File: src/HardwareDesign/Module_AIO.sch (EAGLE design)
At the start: 284 parts, among them IC1 MIC5504-3.3YM5-TR, IC10 ADS9234RIRHBR, IC11 AD8605, IC12 MCP1525T-I/TT, IC13 AD8605, IC14 TPS65131, IC15 TPS7A39, IC16 SN74LVC2G66, IC17 74LVC1G04, IC22 DAC8568, IC23 AD8605, IC24 OPA192, IC25 OPA192, IC26 OPA192, IC27 OPA192, IC28 OPA197, IC29 OPA197, IC30 OPA197, IC31 OPA197, IC6 DG409, IC7 ADA4254ACPZ, IC8 DG409, IC9 ADA4254ACPZ, T2 IRLML5203, X1 MAB64

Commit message: AIO Board ready
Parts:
- removed SPI0_MISO, SPI0_MOSI, SPI0_SCK: TP, ds_passive:TP
- added AVDD, DVDD, IOVDD, VBUS, VREF1: TP, ds_passive:TP
- added C112, C113, C114, C116, C16, C17, C18, C77, C80, C81, C82, C83, C84, C87, C88, C89: 100nF, ds_passive:C-0402
- added C115: 4.7nF, ds_passive:C0402
- added C15: 1uF, ds_passive:C-0402
- added C19, C20: 15pF, ds_passive:C-0402
- added C78: 10uF, ds_passive:C0805
- added C79: 100nF, ds_passive:C0402
- added D1: SS12, Diodes:SS12
- added DBG1, DBG2: (no value), ds_con:CON-1X4
- added ESD1: SP0503BAHTG-ES, ds_ic_peripherals:SP0503BAHT
- added IC2: RP2040, ds_ic_mcu:RP2040
- added IC3: MCP6001AIDBVRG, ds_ic_opa:MCP6001RT
- added IC4: W25Q128JVPIQ, MCU:W25Q128JVP
- added J1: (no value), ds_con:N10236-52B3PC
- added JP-3V3-1, JP-3V3-2: 0R, ds_passive:R0603
- added R10, R11: 1K, ds_passive:R0402
- added R12: 2.2K 1%, ds_passive:R0402
- added R13, R39: 27R, ds_passive:R0402
- added R17, R72, R77: 4.7K, ds_passive:R0402
- added R18: DNI, ds_passive:R0402
- added R61, R62: 5.1K, ds_passive:R0402
- added R63, R64, R75: 10K, ds_passive:R0402
- added R67, R71: 10K 0.1%, ds_passive:R0402
- added R68: 1M, ds_passive:R0402
- added R69, R70: 100K 0.1%, ds_passive:R0402
- added R9: 0R, ds_passive:R0402
- added REF1: LM4040BXX, ds_ic_vreg:LM4040BXX
- added RESET, USB_BOOT: B3U-1000P-B, 52101-101-REV-A_v16:SWITCH-OMRON_B3U-1000P
- added USBC: USB-TYPE-C-018, Wurth_Connectors_WR-USB:629722000214
- added X2: K5A1200015304P, ds_passive:CRYSTAL
- C102, C104, C108, C109, C93, C94, C95, C96, C97, C98: device ds_passive:C-0402 -> ds_passive:C-0805
- R26, R27, R28, R29, R30, R31, R32, R34, R35, R36, R37, R38, R40, R41: device ds_passive:R0603 -> ds_passive:R0402
- R55, R56: value (none) -> 20K
- X1: value MAB64 -> CON-VG_MAB64; device con-vg:MAB64 -> ds_con:CON-VG_MAB64
- renumbered SPI0_CS0 to CS3, SPI1_CS0 to MOSI, SPI1_CS1 to MISO, SPI1_CS2 to SCK, SPI1_CS3 to CS0, SPI1_CS4 to CS1, SPI1_CS5 to CS2
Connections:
- removed net SPI1_CS0: IC10.!CS, MOSI.P$1, R15.1, X1A.2
- removed net SPI1_CS1: IC7.!CS, MISO.P$1, X1A.3
- removed net SPI1_CS2: IC9.!CS, SCK.P$1, X1A.4
- new net !QSPI_SS: IC2.QSPI_SS_N, IC4.!CS, R11.2, R18.1
- new net +1V1: C112.1, C113.1, C114.1, DVDD.P$1, IC2.DVDD, IC2.VREG_VOUT
- new net ADC_12VN: IC2.GPIO28/ADC2, R67.2, R69.1
- new net ADC_12VP: IC2.GPIO27/ADC1, R70.2, R71.1
- new net ADC_5VP: IC2.GPIO29/ADC3, R72.1, R77.2
- new net ADC_VUSB: IC2.GPIO26/ADC0, R63.2, R64.1
- new net AVDD: AVDD.P$1, C17.1, C89.1, IC2.ADC_AVDD, IC3.-IN, IC3.OUT
- new net CC1: R62.1, USBC.CC1
- new net CC2: R61.1, USBC.CC2
- new net EXT: J1.1, J1.20
- new net N$1: C20.1, R10.1, R9.2, X2.OUT
- new net N$4: JP-3V3-1.2, X1A.1
- new net N$6: JP-3V3-2.2, X1B.1
- new net QSPI_SCLK: IC2.QSPI_SCLK, IC4.CLK
- new net QSPI_SD0: IC2.QSPI_SD0, IC4.DI/IO0
- new net QSPI_SD1: IC2.QSPI_SD1, IC4.DO/IO1
- new net QSPI_SD2: IC2.QSPI_SD2, IC4.!WP!/IO2
- new net QSPI_SD3: IC2.QSPI_SD3, IC4.!HOLD!/IO3
- new net RP2040_RST: IC2.RUN, R75.2, RESET.P, X1B.18
- new net RP_USBD_N: IC2.USB_DM, R13.2
- new net RP_USBD_P: IC2.USB_DP, R39.2
- new net RP_XI: C19.1, IC2.XIN, R9.1, X2.CON
- new net RP_XO: IC2.XOUT, R10.2
- new net SDO_A_1: IC10.SDO-1/1A, IC2.GPIO17, X1A.18
- new net SDO_A_2: IC10.SDO-2/2A, IC2.GPIO18, X1A.19
- new net SDO_A_3: IC10.SDO-3/3A, IC2.GPIO19, X1A.20
- new net SDO_B_1: IC10.SDO-5/1B, IC2.GPIO21, X1A.22
- new net SDO_B_2: IC10.SDO-6/2B, IC2.GPIO22, X1A.23
- new net SDO_B_3: IC10.SDO-7/3B, IC2.GPIO23, X1A.24
- new net SPI0_CS1: CS1.P$1, IC2.GPIO6, IC7.!CS, X1A.3
- new net SPI0_CS2: CS2.P$1, IC2.GPIO7, IC9.!CS, X1A.4
- new net SPI0_CS3: CS3.P$1, IC2.GPIO25, IC22.!SYNC, R86.3, X1B.2
- new net SPI1_CS: IC2.GPIO13, X1A.29, X1B.29
- new net SWCLK: DBG2.P$1, IC2.SWCLK, X1B.23
- new net SWDIO: DBG2.P$3, IC2.SWDIO, X1B.24
- new net UART0_RX: DBG1.P$1, IC2.GPIO0, X1B.20
- new net UART0_TX: DBG1.P$3, IC2.GPIO1, X1B.21
- new net USBD_N: ESD1.C2, R13.1, USBC.D-1, USBC.D-2
- new net USBD_P: ESD1.C1, R39.1, USBC.D+1, USBC.D+2
- new net USB_BOOT: R11.1, USB_BOOT.P
- new net USB_SHIELD: C115.1, R68.1, USBC.SHIELD
- new net VBUS: C78.1, C79.1, D1.A, ESD1.C3, R12.1, R63.1, USBC.VBUS, USBC.VBUS1, USBC.VBUS2, USBC.VBUS3, VBUS.P$1
- new net VREF: C15.1, C16.1, IC3.+IN, R17.1, REF1.C, VREF1.P$1
- net !ADC_RST: now also IC2.GPIO9
- net +12V: now also R70.1
- net +3V3: now also C116.1, C18.1, C77.1, C80.1, C81.1, C82.1, C83.1, C84.1, C87.1, C88.1, IC2.IOVDD, IC2.USB_VDD, IC2.VREG_VIN, IC3.V+, IC4.VCC, IOVDD.P$1, JP-3V3-1.1, JP-3V3-2.1, R17.2, R18.2, R75.1; no longer X1A.1, X1B.1
- net +5V: now also D1.C, R72.2, X1A.8, X1A.9, X1B.8, X1B.9; no longer X1B.13, X1B.14
- net -12V: now also R67.1
- net ADC_RDY: now also IC2.GPIO8
- net AI_0+: now also J1.2; no longer X1A.17
- net AI_1-: now also J1.3; no longer X1A.18
- net AI_10+: now also J1.12; no longer X1A.27
- net AI_11-: now also J1.13; no longer X1A.28
- net AI_12+: now also J1.14; no longer X1A.29
- net AI_13-: now also J1.15; no longer X1A.30
- net AI_14+: now also J1.16; no longer X1A.31
- net AI_15-: now also J1.17; no longer X1A.32
- net AI_2+: now also J1.4; no longer X1A.19
- net AI_3-: now also J1.5; no longer X1A.20
- net AI_4+: now also J1.6; no longer X1A.21
- net AI_5-: now also J1.7; no longer X1A.22
- net AI_6+: now also J1.8; no longer X1A.23
- net AI_7-: now also J1.9; no longer X1A.24
- net AI_8+: now also J1.10; no longer X1A.25
- net AI_9-: now also J1.11; no longer X1A.26
- net AO_0: now also J1.21; no longer X1B.25
- net AO_1: now also J1.23; no longer X1B.26
- net AO_2: now also J1.25; no longer X1B.27
- net AO_3: now also J1.27; no longer X1B.28
- net AO_4: now also J1.29; no longer X1B.29
- net AO_5: now also J1.31; no longer X1B.30
- net AO_6: now also J1.33; no longer X1B.31
- net AO_7: now also J1.35; no longer X1B.32
- net DAC_!CLR: now also IC2.GPIO15, X1B.13; no longer X1B.10
- net DAC_!LDAC: now also IC2.GPIO14, X1B.12; no longer X1B.9
- net GND: now also C112.2, C113.2, C114.2, C115.2, C116.2, C15.2, C16.2, C17.2, C18.2, C19.2, C20.2, C77.2, C78.2, C79.2, C80.2, C81.2, C82.2, C83.2, C84.2, C87.2, C88.2, C89.2, DBG1.P$2, DBG1.P$4, DBG2.P$2, DBG2.P$4, ESD1.A, IC2.GND, IC2.TESTEN, IC3.V-, IC4.GND, J1.18, J1.19, J1.22, J1.24, J1.26, J1.28, J1.30, J1.32, J1.34, J1.36, J1.MH1, J1.MH2, R12.2, R61.2, R62.2, R64.2, R68.2, R69.2, R71.2, R77.1, REF1.A, RESET.S, USBC.GND, USBC.GND1, USBC.GND2, USBC.GND3, USB_BOOT.S, X1A.25, X1A.30, X1A.31, X1A.32, X1B.10, X1B.14, X1B.15, X1B.16, X1B.19, X1B.22, X1B.25, X1B.30, X1B.31, X1B.32, X2.VDD, X2.VSS; no longer X1B.11, X1B.12, X1B.23, X1B.24
- net MISO_SEL: now also IC2.GPIO24
- net SDO_A_0: now also IC2.GPIO16, X1A.17; no longer X1A.9
- net SDO_B_0: now also IC2.GPIO20, X1A.21; no longer X1A.8
- net SPI0_CS0: now also CS0.P$1, IC10.!CS, IC2.GPIO5, R15.1, X1A.2; no longer CS3.P$1, IC22.!SYNC, R86.3, X1B.2
- net SPI0_MISO: now also IC16.1B, IC16.2B, IC2.GPIO4, IC7.SDO, IC9.SDO, MISO.P$1, X1A.7, X1B.7; no longer SPI0_MISO.P$1, X1B.5
- net SPI0_MOSI: now also IC10.SDI, IC2.GPIO3, IC7.SDI, IC9.SDI, MOSI.P$1, X1A.6, X1B.6; no longer SPI0_MOSI.P$1, X1B.4
- net SPI0_SCK: now also IC10.SCLK, IC2.GPIO2, IC7.SCK, IC9.SCK, SCK.P$1, X1A.5, X1B.5; no longer SPI0_SCK.P$1, X1B.3
- net SPI1_MISO: now also IC2.GPIO12, X1A.26, X1B.26; no longer CS1.P$1, IC16.1B, IC16.2B, IC7.SDO, IC9.SDO, X1A.7
- net SPI1_MOSI: now also IC2.GPIO11, X1A.27, X1B.27; no longer CS0.P$1, IC10.SDI, IC7.SDI, IC9.SDI, X1A.6
- net SPI1_SCK: now also IC2.GPIO10, X1A.28, X1B.28; no longer CS2.P$1, IC10.SCLK, IC7.SCK, IC9.SCK, X1A.5
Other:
- note added: "12MHZ CRYSTAL"
- note added: "ADC VREF"
- note added: "ANALOG CONNECTOR"
- note added: "BOARD CONNECTOR"
- note added: "Controller Board"
- note added: "DEBUG"
- note added: "DECOUPLING"
- note added: "David Sipos / DvidMakesThings"
- note added: "EXTERNAL SUPPLY"
- note added: "Enable SWD Debugging on Raspberry Pi: Install OpenOCD (sudo apt install openocd) Configure /boot/config.txt to enable GPIO-based debugging."
- note added: "NOT YET IPLEMENTED"
- note added: "RP2040 FLASH"
- note added: "RP2040 MCU"
- note added: "Rev 1.0"
- note added: "USB-C CONNECTOR"

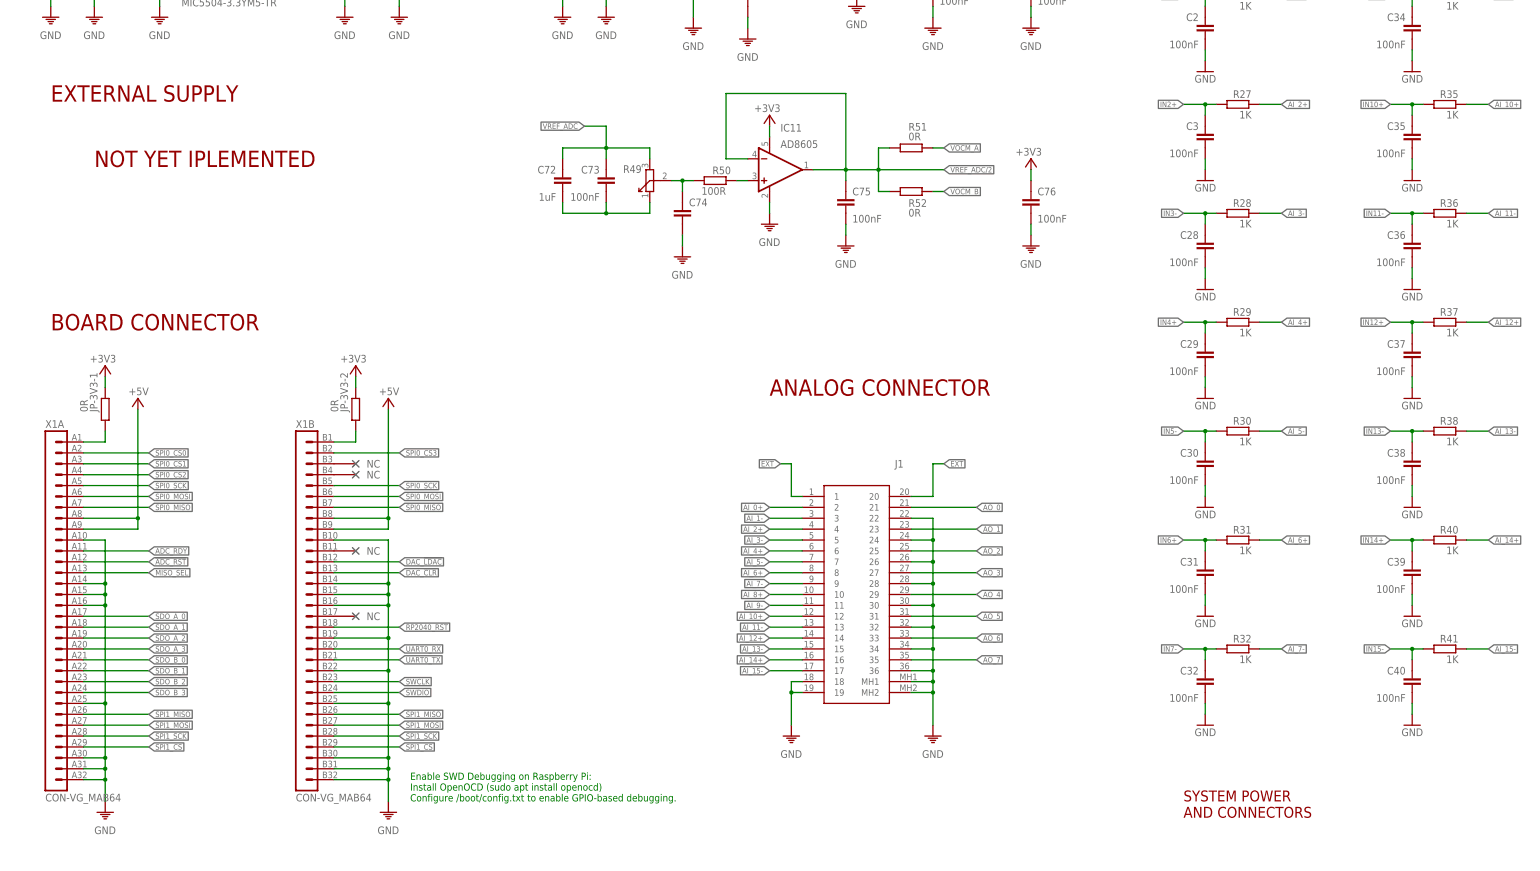
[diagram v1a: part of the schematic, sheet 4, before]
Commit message: finish DIO card desing
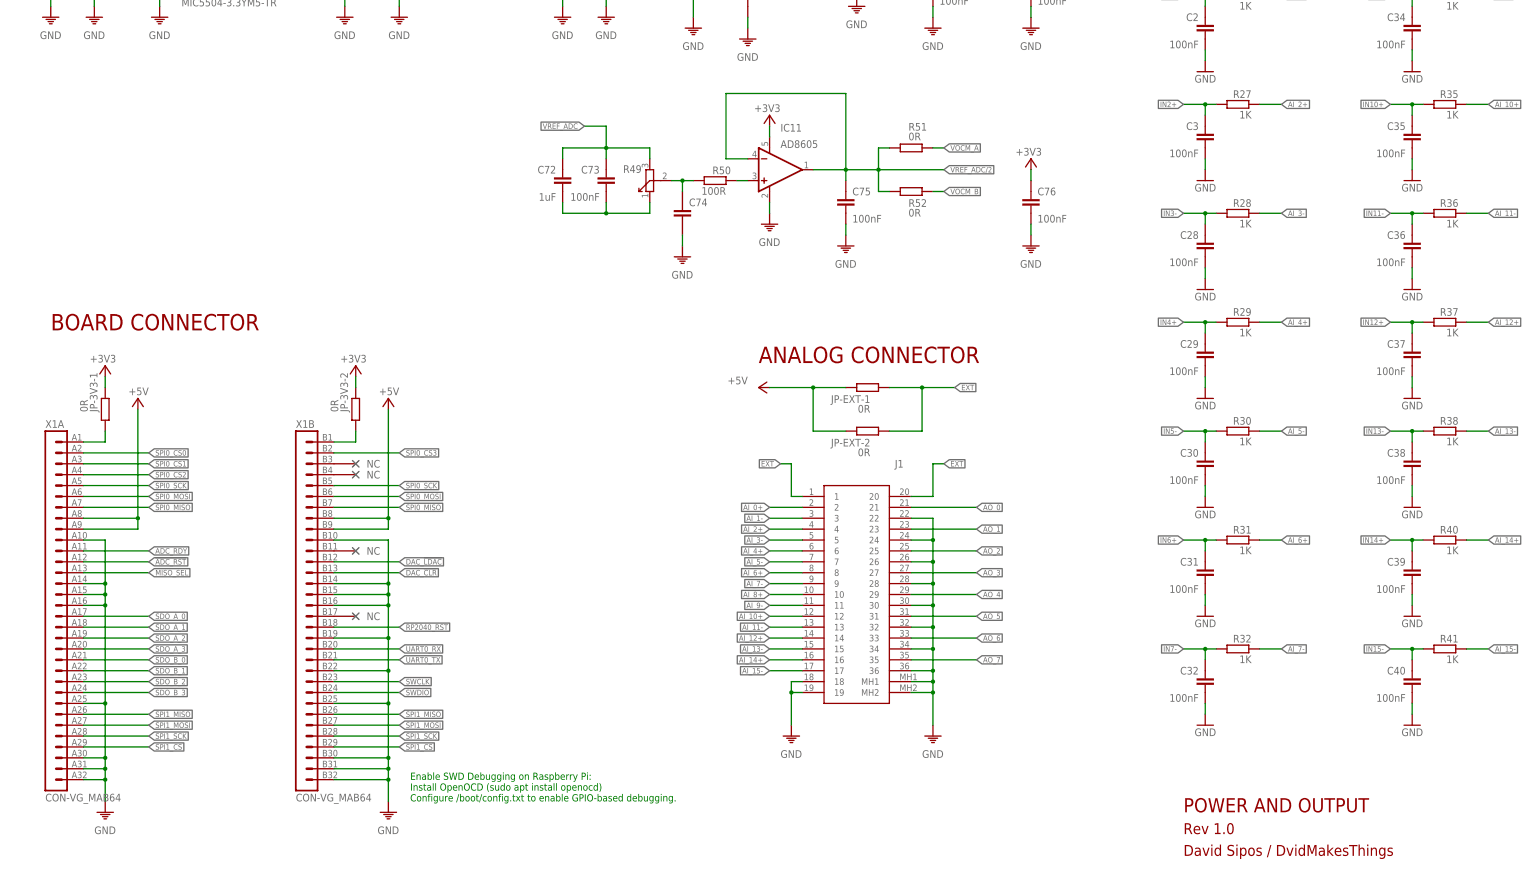
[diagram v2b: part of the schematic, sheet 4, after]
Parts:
- added JP-EXT-1, JP-EXT-2: 0R, ds_passive:R0603
- R72, R77: value 4.7K -> 10K
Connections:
- net +5V: now also JP-EXT-1.1, JP-EXT-2.1
- net EXT: now also JP-EXT-1.2, JP-EXT-2.2
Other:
- note added: "ANALOG IN"
- note added: "DAC"
- note added: "DC-DC CONV"
- note added: "POWER AND OUTPUT"
- note removed: "ADC ON SPI1"
- note removed: "AI-POWER"
- note removed: "ANALOG INPUT"
- note removed: "ANALOG OUTPUT"
- note removed: "Controller Board"
- note removed: "EXTERNAL SUPPLY"
- note removed: "NOT YET IPLEMENTED"
- note removed: "SYSTEM POWER AND CONNECTORS"
